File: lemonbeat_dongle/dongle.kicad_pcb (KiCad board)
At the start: 4 copper layers, 50 x 20 mm, 82 parts, among them J201 USB_A, J202 Prog, J203 u.FL, J301 SMA, SW201 SW_Push, U201 nRF52840, U301 Si4467, Y201 32MHz, Y202 32.768kHz, Y301 26MHz

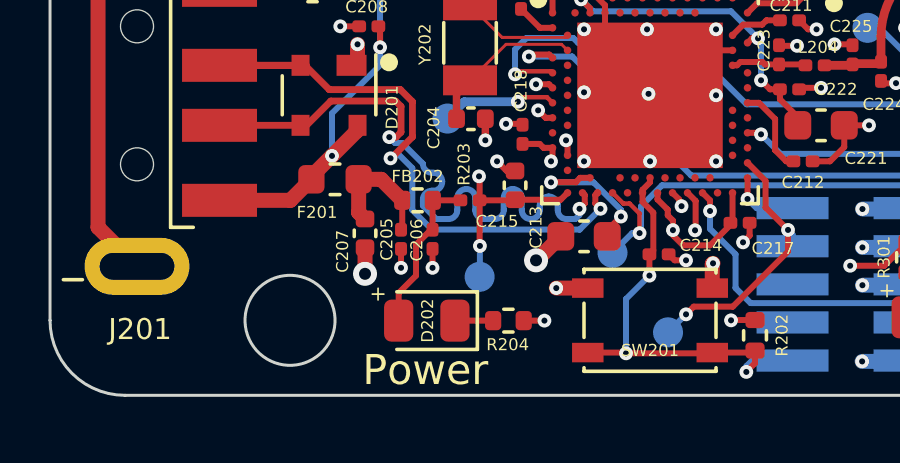
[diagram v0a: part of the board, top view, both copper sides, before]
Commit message: dongle: PCB: move power LED even further away from hole
This is to avoid a shortcut between the LED pad (VDD) and the case.

Note: the GND via that is closer to the hole is less problematic, as the
case is already on GND potential.
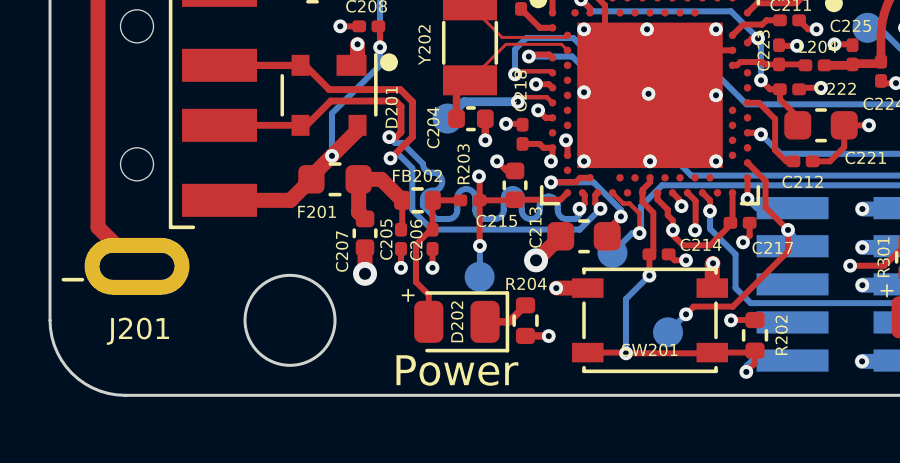
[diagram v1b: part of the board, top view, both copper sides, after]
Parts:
- moved D202 1.00 mm to (124.1, 111.5)
- moved R204 0.57 mm to (126.3, 111.5), turned to -90 degrees
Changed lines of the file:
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@@
   )
   (footprint "LED_SMD:LED_0805_2012Metric" (layer "F.Cu")
-    (at 123.06 111.51 180)
+    (at 124.0625 111.55 180)
     (descr "LED SMD 0805 (2012 Metric), square (rectangular) end terminal, IPC_7351 nominal, (Body size source: https://docs.google.com/spreadsheets/d/1BsfQQcO9C6DZCsRaXUlFlo91Tg2WpOkGARC1WS5S8t0/edit?usp=sharing), generated with kicad-footprint-generator")
     (tags "LED")
@@
   )
   (footprint "Resistor_SMD:R_0402_1005Metric" (layer "F.Cu")
-    (at 125.78 111.51)
+    (at 126.35 111.51 -90)
     (descr "Resistor SMD 0402 (1005 Metric), square (rectangular) end terminal, IPC_7351 nominal, (Body size source: IPC-SM-782 page 72, https://www.pcb-3d.com/wordpress/wp-content/uploads/ipc-sm-782a_amendment_1_and_2.pdf), generated with kicad-footprint-generator")
     (tags "resistor")
@@
     (property "ki_keywords" "R res resistor")
     (attr smd)
-    (fp_text reference "R204" (at -0.025 0.8) (layer "F.SilkS")
+    (fp_text reference "R204" (at -1.21 -0.02 -180) (layer "F.SilkS")
         (effects (font (size 0.4 0.4) (thickness 0.1)))
     )
-    (fp_text value "5k6" (at 0 1.17) (layer "F.Fab")
+    (fp_text value "5k6" (at 0 1.17 90) (layer "F.Fab")
         (effects (font (size 1 1) (thickness 0.15)))
     )
-    (fp_text user "${REFERENCE}" (at 0 0) (layer "F.Fab")
+    (fp_text user "${REFERENCE}" (at 0 0 90) (layer "F.Fab")
         (effects (font (size 0.26 0.26) (thickness 0.04)))
     )
@@
     (fp_line (start 0.525 0.27) (end -0.525 0.27)
       (stroke (width 0.1) (type solid)) (layer "F.Fab"))
-    (pad "1" smd roundrect (at -0.51 0) (size 0.54 0.64) (layers "F.Cu" "F.Paste" "F.Mask") (roundrect_rratio 0.25)
+    (pad "1" smd roundrect (at -0.51 0 270) (size 0.54 0.64) (layers "F.Cu" "F.Paste" "F.Mask") (roundrect_rratio 0.25)
       (net 29 "Net-(D202-K)") (pintype "passive"))
-    (pad "2" smd roundrect (at 0.51 0) (size 0.54 0.64) (layers "F.Cu" "F.Paste" "F.Mask") (roundrect_rratio 0.25)
+    (pad "2" smd roundrect (at 0.51 0 270) (size 0.54 0.64) (layers "F.Cu" "F.Paste" "F.Mask") (roundrect_rratio 0.25)
       (net 1 "GND") (pintype "passive"))
     (model "${KICAD6_3DMODEL_DIR}/Resistor_SMD.3dshapes/R_0402_1005Metric.wrl"
@@
   (gr_line (start 113 94) (end 158 94)
     (stroke (width 0.1) (type solid)) (layer "Edge.Cuts"))
-  (gr_text "Power" (at 123.01 113.16) (layer "F.SilkS")
+  (gr_text "Power" (at 124.0125 113.2) (layer "F.SilkS")
     (effects (font (size 1 1) (thickness 0.15)))
   )
-  (gr_text "+" (at 121.435 110.61) (layer "F.SilkS")
+  (gr_text "+" (at 122.4375 110.65) (layer "F.SilkS")
     (effects (font (size 0.5 0.5) (thickness 0.1)))
   )
@@
   (segment (start 129 101) (end 128.7 100.7) (width 0.2) (layer "F.Cu") (net 1))
   (segment (start 147.5 95.25) (end 149.25 95.25) (width 0.5) (layer "F.Cu") (net 1))
+  (segment (start 127.12 112.02) (end 127.125 112.025) (width 0.25) (layer "F.Cu") (net 1))
   (segment (start 138.7 103.5935) (end 138.6935 103.6) (width 0.2) (layer "F.Cu") (net 1))
   (segment (start 140.5 95) (end 142.2 95) (width 0.25) (layer "F.Cu") (net 1))
@@
   (segment (start 136.88 97.2) (end 136.89 97.21) (width 0.2) (layer "F.Cu") (net 1))
   (segment (start 142.7875 105.3125) (end 142.7875 104.45) (width 0.2) (layer "F.Cu") (net 1))
-  (segment (start 126.98 111.51) (end 126.29 111.51) (width 0.2) (layer "F.Cu") (net 1))
   (segment (start 120.7 101.7) (end 120.75 101.75) (width 0.2) (layer "F.Cu") (net 1))
   (segment (start 137.56 98.71) (end 137.56 98) (width 0.2) (layer "F.Cu") (net 1))
@@
   (segment (start 144.58 100.3) (end 144.58 99.42) (width 0.5) (layer "F.Cu") (net 1))
   (segment (start 136.19 97.2) (end 136.88 97.2) (width 0.2) (layer "F.Cu") (net 1))
+  (segment (start 126.35 112.02) (end 127.12 112.02) (width 0.25) (layer "F.Cu") (net 1))
   (segment (start 129 101.25) (end 129 101) (width 0.2) (layer "F.Cu") (net 1))
   (segment (start 128.7 100.7) (end 128.7 100.15) (width 0.2) (layer "F.Cu") (net 1))
@@
   (via (at 154.625 111.875) (size 0.46) (drill 0.2) (layers "F.Cu" "B.Cu") (free) (net 1))
   (via (at 125.7 104.95) (size 0.46) (drill 0.2) (layers "F.Cu" "B.Cu") (free) (net 1))
-  (via (at 126.98 111.51) (size 0.46) (drill 0.2) (layers "F.Cu" "B.Cu") (free) (net 1))
+  (via (at 127.125 112.025) (size 0.46) (drill 0.2) (layers "F.Cu" "B.Cu") (free) (net 1))
   (via (at 126.2 99.85) (size 0.46) (drill 0.2) (layers "F.Cu" "B.Cu") (free) (net 1))
   (via (at 136.05 101.8) (size 0.46) (drill 0.2) (layers "F.Cu" "B.Cu") (free) (net 1))
@@
   (segment (start 120.7875 106.8) (end 120.7875 107.9075) (width 0.5) (layer "F.Cu") (net 6))
   (segment (start 123.25 107.51) (end 123.26 107.5) (width 0.2) (layer "F.Cu") (net 7))
-  (segment (start 122.7 108.977552) (end 123.197552 108.48) (width 0.2) (layer "F.Cu") (net 7))
-  (segment (start 122.1225 110.5875) (end 122.7 110.01) (width 0.2) (layer "F.Cu") (net 7))
   (segment (start 123.26 107.5) (end 124.18 107.5) (width 0.2) (layer "F.Cu") (net 7))
+  (segment (start 122.7 110.225) (end 123.125 110.65) (width 0.2) (layer "F.Cu") (net 7))
+  (segment (start 123.197552 108.48) (end 122.7 108.977552) (width 0.2) (layer "F.Cu") (net 7))
+  (segment (start 122.7 108.977552) (end 122.7 110.225) (width 0.2) (layer "F.Cu") (net 7))
   (segment (start 123.25 108.48) (end 123.25 107.51) (width 0.2) (layer "F.Cu") (net 7))
-  (segment (start 122.1225 111.51) (end 122.1225 110.5875) (width 0.2) (layer "F.Cu") (net 7))
-  (segment (start 122.7 110.01) (end 122.7 108.977552) (width 0.2) (layer "F.Cu") (net 7))
+  (segment (start 123.125 110.65) (end 123.125 111.55) (width 0.2) (layer "F.Cu") (net 7))
   (segment (start 119.2125 106.8) (end 119.2125 106.704908) (width 0.5) (layer "F.Cu") (net 8))
   (segment (start 120.75 105) (end 120.75 105.167408) (width 0.5) (layer "F.Cu") (net 8))
@@
   (segment (start 122.576803 106.425989) (end 122.094359 105.943545) (width 0.2) (layer "B.Cu") (net 28))
   (segment (start 122.094359 105.943545) (end 122.006455 105.943545) (width 0.2) (layer "B.Cu") (net 28))
-  (segment (start 123.9975 111.51) (end 125.27 111.51) (width 0.2) (layer "F.Cu") (net 29))
+  (segment (start 125.8 111.55) (end 126.35 111) (width 0.25) (layer "F.Cu") (net 29))
+  (segment (start 125 111.55) (end 125.8 111.55) (width 0.25) (layer "F.Cu") (net 29))
   (segment (start 140.9125 111.4) (end 140.9125 111.2125) (width 0.2) (layer "F.Cu") (net 30))
   (segment (start 139.61 109.91) (end 139.1 109.91) (width 0.2) (layer "F.Cu") (net 30))

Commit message: dongle: update date & revision; typo fix
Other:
- board text added: "Rev. 0.3.0"
- board text removed: "Rev. 0.2.0"
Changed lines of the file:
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@@
     (effects (font (size 0.5 0.5) (thickness 0.1)))
   )
-  (gr_text "Rev. 0.2.0" (at 150.6 110.5) (layer "F.SilkS")
+  (gr_text "Rev. 0.3.0" (at 150.6 110.5) (layer "F.SilkS")
     (effects (font (size 1 1) (thickness 0.15)))
   )

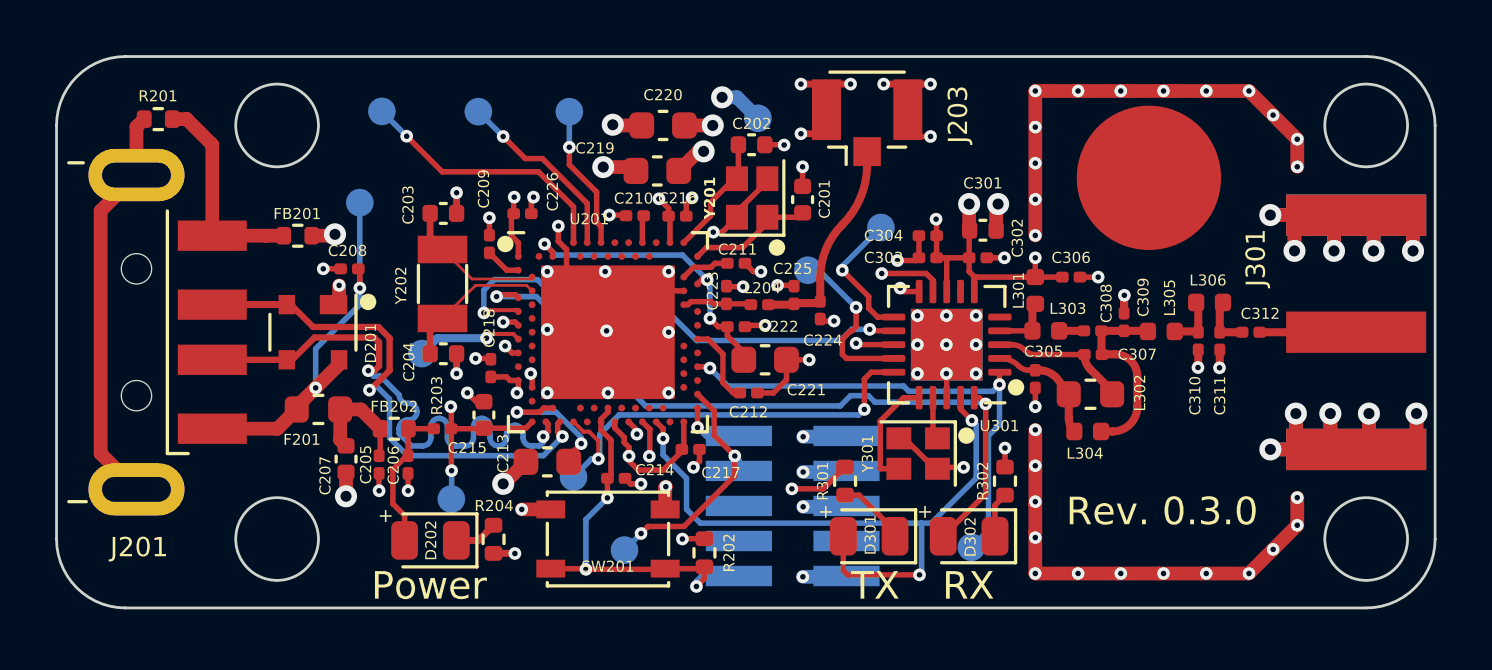
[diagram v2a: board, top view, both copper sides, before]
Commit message: dongle: PCB: silk screen rings around holes & clear gap
- rings in the silk screen now indicate the space occupied by the
  cylinder of the case
- C207, via & a PCB trace are move a bit further away from the holes
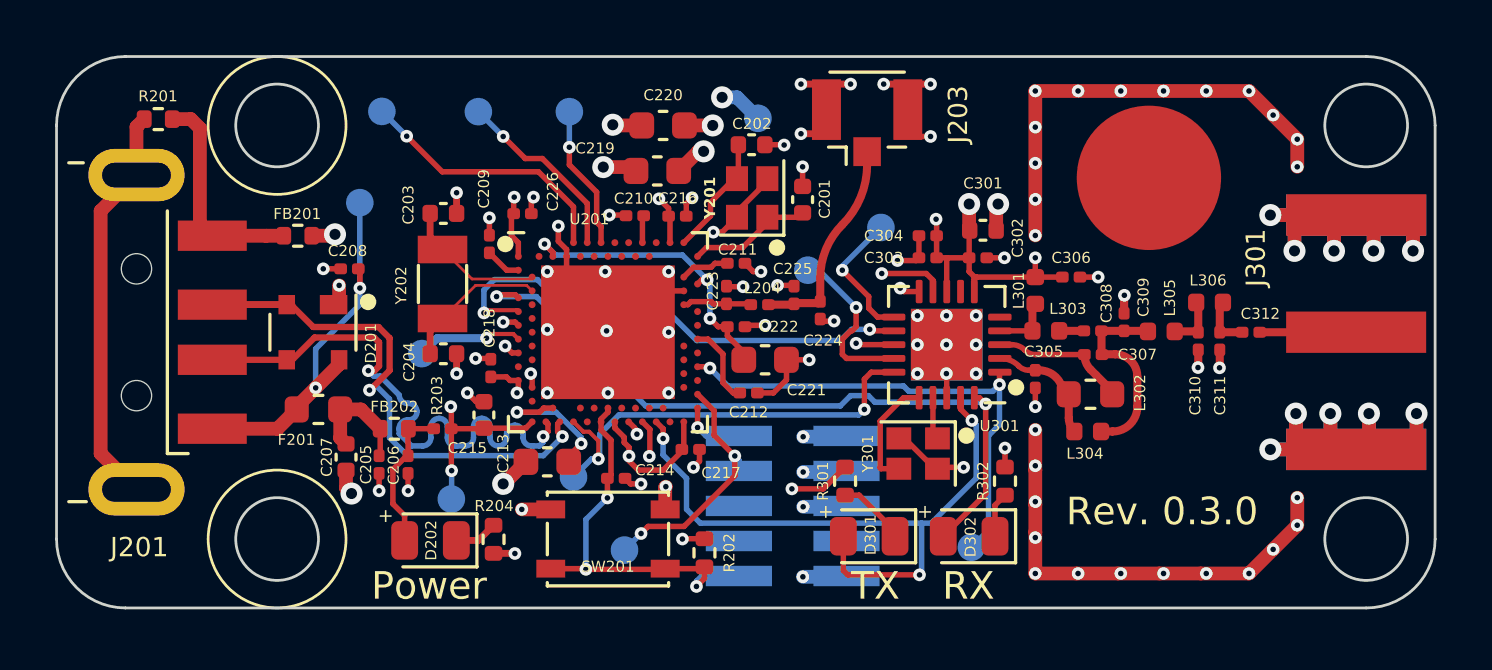
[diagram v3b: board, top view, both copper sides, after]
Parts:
- moved C207 0.07 mm to (121.0, 108.5)
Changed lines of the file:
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@@
   )
   (footprint "Capacitor_SMD:C_0402_1005Metric" (layer "F.Cu")
-    (at 121 108.6 -90)
+    (at 121 108.53 -90)
     (descr "Capacitor SMD 0402 (1005 Metric), square (rectangular) end terminal, IPC_7351 nominal, (Body size source: IPC-SM-782 page 76, https://www.pcb-3d.com/wordpress/wp-content/uploads/ipc-sm-782a_amendment_1_and_2.pdf), generated with kicad-footprint-generator")
     (tags "capacitor")
@@
     (property "ki_keywords" "cap capacitor")
     (attr smd)
-    (fp_text reference "C207" (at 0.6 0.75 -90) (layer "F.SilkS")
+    (fp_text reference "C207" (at 0 0.7 -90) (layer "F.SilkS")
         (effects (font (size 0.4 0.4) (thickness 0.1)))
     )
@@
     (property "ki_keywords" "resettable fuse PTC PPTC polyfuse polyswitch")
     (attr smd)
-    (fp_text reference "F201" (at 0.6 -1.1) (layer "F.SilkS")
+    (fp_text reference "F201" (at 0.8 -1.1) (layer "F.SilkS")
         (effects (font (size 0.4 0.4) (thickness 0.1)))
     )
@@
   (gr_circle (center 150.12 98.4) (end 152.637538 98.4)
     (stroke (width 0.2) (type solid)) (fill solid) (layer "F.Cu"))
+  (gr_circle (center 118.5 96.5) (end 121 96.5)
+    (stroke (width 0.1) (type default)) (fill none) (layer "F.SilkS"))
   (gr_circle (center 136.63 100.93) (end 136.63 101.153607)
     (stroke (width 0.15) (type solid)) (fill solid) (layer "F.SilkS"))
   (gr_circle (center 143.5 107.75) (end 143.723607 107.75)
     (stroke (width 0.15) (type solid)) (fill solid) (layer "F.SilkS"))
+  (gr_circle (center 118.5 111.5) (end 121 111.5)
+    (stroke (width 0.1) (type default)) (fill none) (layer "F.SilkS"))
   (gr_circle (center 145.3 106) (end 145.523607 106)
     (stroke (width 0.15) (type solid)) (fill solid) (layer "F.SilkS"))
@@
   (segment (start 130.45 103.95) (end 130.5 104) (width 0.1) (layer "F.Cu") (net 1))
   (segment (start 136.28 98.526) (end 136.28 98.43) (width 0.2) (layer "F.Cu") (net 1))
+  (segment (start 121 109.65) (end 121.2 109.85) (width 0.5) (layer "F.Cu") (net 1))
   (segment (start 141.78 101.3) (end 141.78 100.5) (width 0.2) (layer "F.Cu") (net 1))
   (segment (start 152.25 95.25) (end 153.75 95.25) (width 0.5) (layer "F.Cu") (net 1))
@@
   (segment (start 146 110.25) (end 146 109) (width 0.5) (layer "F.Cu") (net 1))
   (segment (start 136.975 105) (end 137.8 105) (width 0.2) (layer "F.Cu") (net 1))
-  (segment (start 121 109.95) (end 121 109.08) (width 0.5) (layer "F.Cu") (net 1))
   (segment (start 135.52 103.75) (end 135.47 103.8) (width 0.2) (layer "F.Cu") (net 1))
   (segment (start 136.5 106.2) (end 136.975 105.725) (width 0.2) (layer "F.Cu") (net 1))
@@
   (segment (start 126.7 109.5) (end 126.725 109.5) (width 0.5) (layer "F.Cu") (net 1))
   (segment (start 156.833333 99.891667) (end 156.85 99.875) (width 0.5) (layer "F.Cu") (net 1))
+  (segment (start 121 109.01) (end 121 109.65) (width 0.5) (layer "F.Cu") (net 1))
   (segment (start 149 112.75) (end 147.5 112.75) (width 0.5) (layer "F.Cu") (net 1))
   (segment (start 155.5 97) (end 155.5 98) (width 0.5) (layer "F.Cu") (net 1))
@@
   (via (at 134.3 96.5) (size 0.8) (drill 0.4) (layers "F.Cu" "B.Cu") (free) (net 1))
   (via (at 125.01 98.94) (size 0.46) (drill 0.2) (layers "F.Cu" "B.Cu") (free) (net 1))
-  (via (at 121 109.95) (size 0.8) (drill 0.4) (layers "F.Cu" "B.Cu") (net 1))
+  (via (at 121.2 109.85) (size 0.8) (drill 0.4) (layers "F.Cu" "B.Cu") (net 1))
   (via (at 137.5 96.8) (size 0.46) (drill 0.2) (layers "F.Cu" "B.Cu") (free) (net 1))
   (via (at 137.57 112.87) (size 0.46) (drill 0.2) (layers "F.Cu" "B.Cu") (net 1))
@@
   (segment (start 127.75 102.5) (end 127.55 102.3) (width 0.1) (layer "F.Cu") (net 5))
   (segment (start 124.05 104.78) (end 124.05 103.95) (width 0.25) (layer "F.Cu") (net 5))
-  (segment (start 120.7875 107.9075) (end 121 108.12) (width 0.5) (layer "F.Cu") (net 6))
   (segment (start 122.24 108.44) (end 122.2 108.48) (width 0.2) (layer "F.Cu") (net 6))
   (segment (start 121.54 106.8) (end 122.24 107.5) (width 0.5) (layer "F.Cu") (net 6))
   (segment (start 120.7875 106.8) (end 121.54 106.8) (width 0.5) (layer "F.Cu") (net 6))
+  (segment (start 120.7875 106.8) (end 120.7875 107.8375) (width 0.5) (layer "F.Cu") (net 6))
   (segment (start 122.24 107.5) (end 122.24 108.44) (width 0.2) (layer "F.Cu") (net 6))
-  (segment (start 120.7875 106.8) (end 120.7875 107.9075) (width 0.5) (layer "F.Cu") (net 6))
+  (segment (start 120.7875 107.8375) (end 121 108.05) (width 0.5) (layer "F.Cu") (net 6))
   (segment (start 123.25 107.51) (end 123.26 107.5) (width 0.2) (layer "F.Cu") (net 7))
   (segment (start 123.26 107.5) (end 124.18 107.5) (width 0.2) (layer "F.Cu") (net 7))
@@
   (segment (start 144.5375 111.4) (end 144.5375 110.2725) (width 0.2) (layer "F.Cu") (net 33))
   (segment (start 144.5375 110.2725) (end 144.9 109.91) (width 0.2) (layer "F.Cu") (net 33))
+  (segment (start 114.7 96.27) (end 115.37 96.27) (width 0.5) (layer "F.Cu") (net 34))
   (segment (start 116.35 100.5) (end 118.1 100.5) (width 0.5) (layer "F.Cu") (net 34))
-  (segment (start 115.22 96.27) (end 116.15 97.2) (width 0.5) (layer "F.Cu") (net 34))
-  (segment (start 114.7 96.27) (end 115.22 96.27) (width 0.5) (layer "F.Cu") (net 34))
-  (segment (start 116.15 97.2) (end 116.15 100.5) (width 0.5) (layer "F.Cu") (net 34))
+  (segment (start 115.7 100.05) (end 116.15 100.5) (width 0.5) (layer "F.Cu") (net 34))
+  (segment (start 115.7 96.6) (end 115.7 100.05) (width 0.5) (layer "F.Cu") (net 34))
+  (segment (start 115.37 96.27) (end 115.7 96.6) (width 0.5) (layer "F.Cu") (net 34))
   (segment (start 118.1 100.5) (end 118.74 100.5) (width 0.5) (layer "F.Cu") (net 34))
   (segment (start 112.1 99.6) (end 113.4 98.3) (width 0.5) (layer "F.Cu") (net 35))
